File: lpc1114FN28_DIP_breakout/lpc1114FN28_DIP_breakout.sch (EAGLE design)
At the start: 17 parts, among them Q1 12MHz

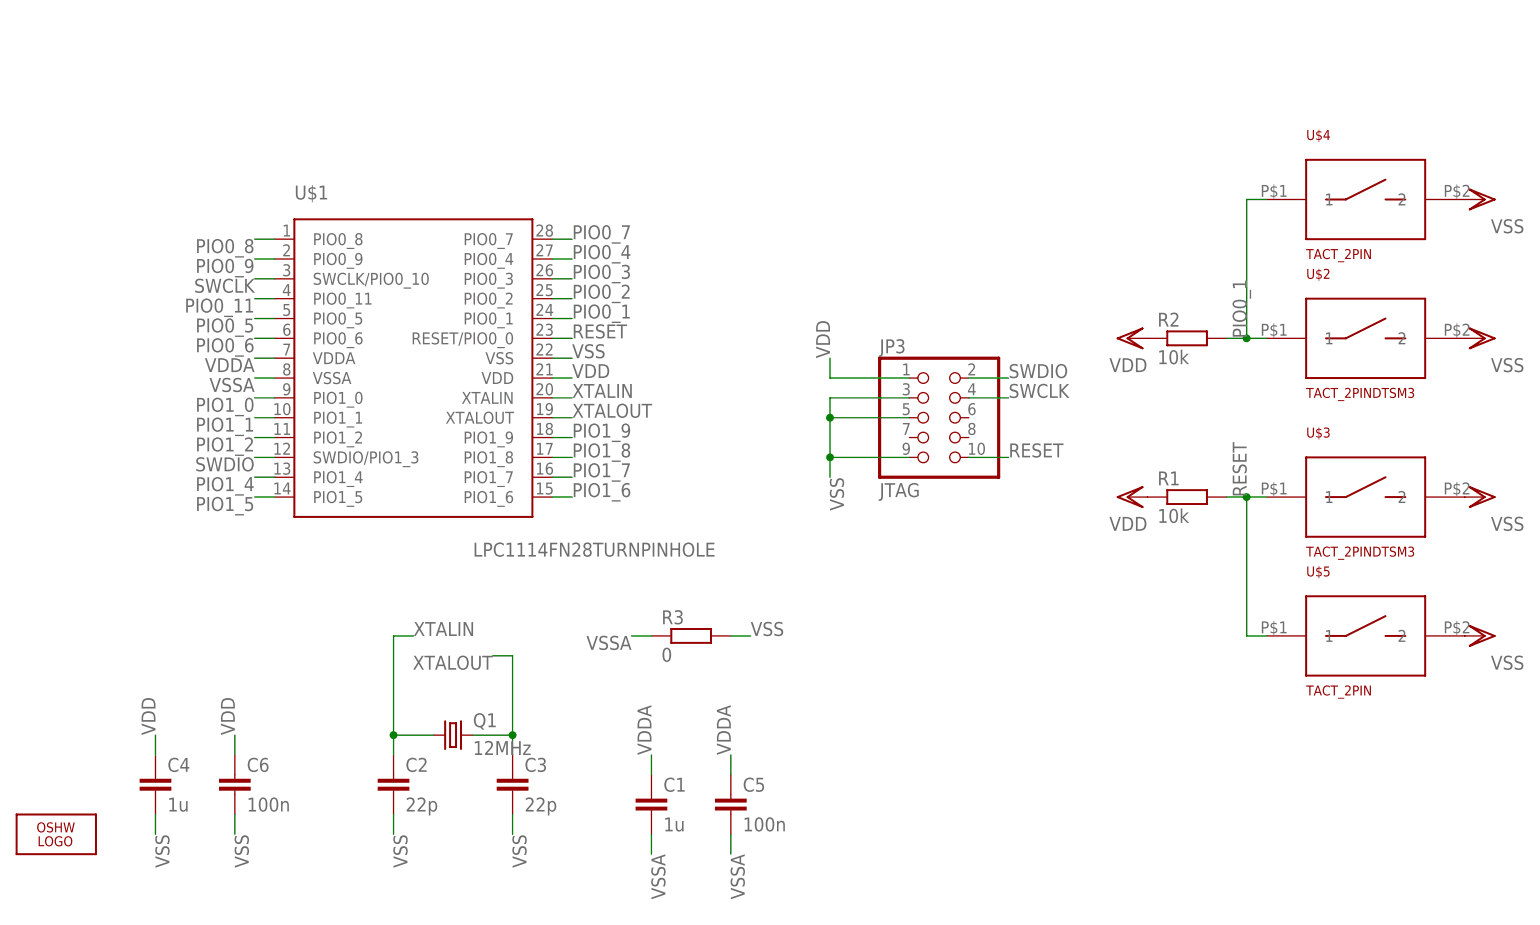
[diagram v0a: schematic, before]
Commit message: * more work on LPC1114FN28 PDIP breakout
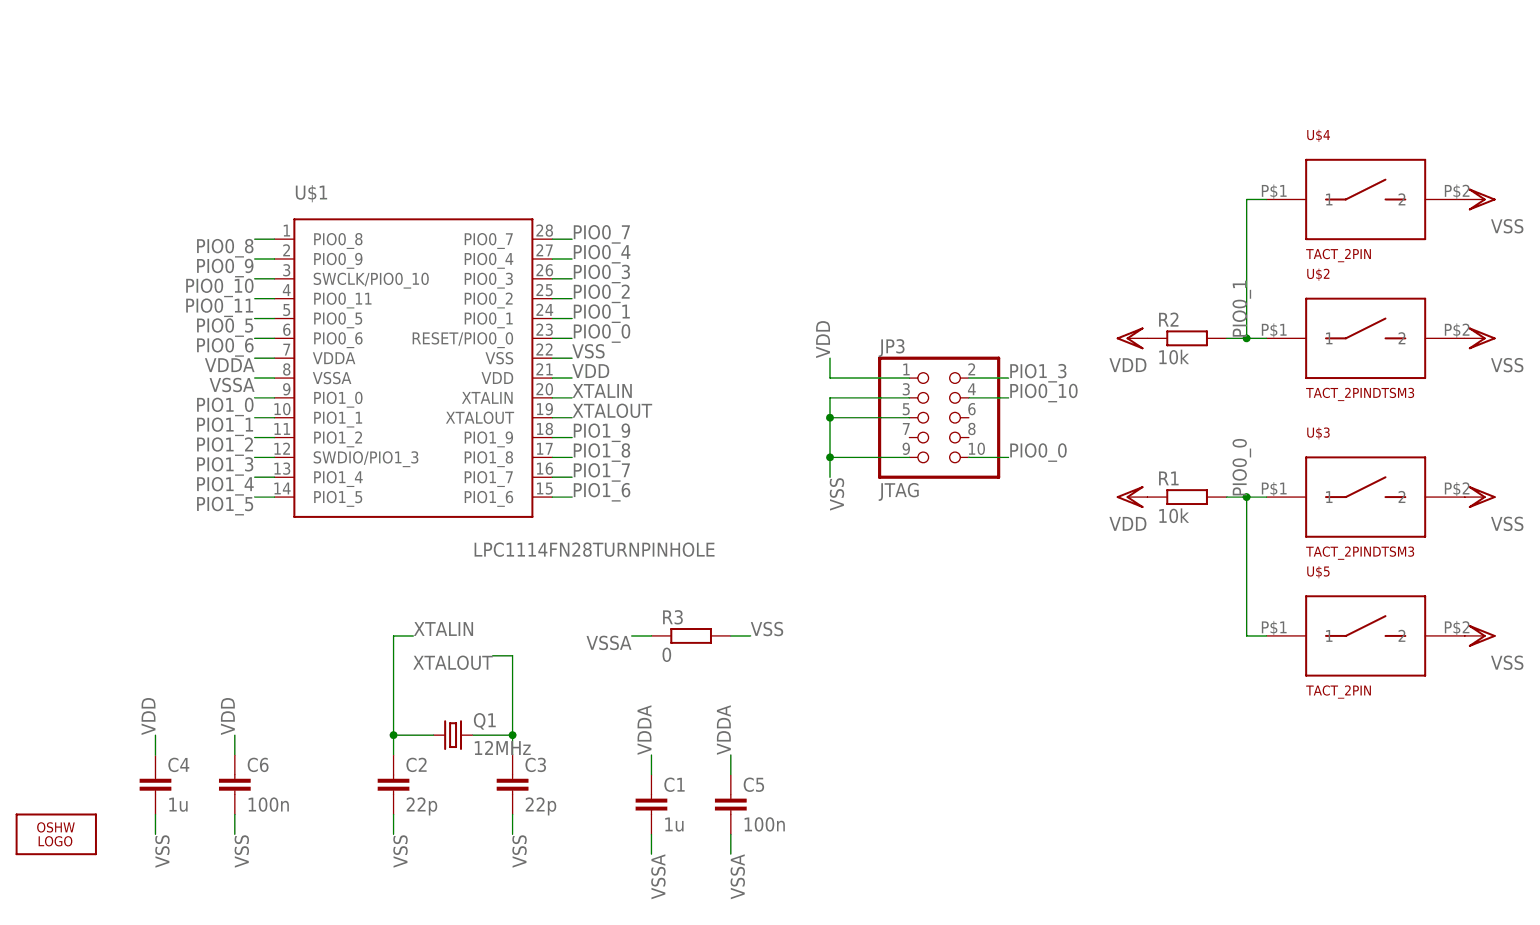
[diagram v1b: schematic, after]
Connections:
- net RESET renamed PIO0_0
- net SWCLK renamed PIO0_10
- net SWDIO renamed PIO1_3
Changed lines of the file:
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@@
-</segment>
-</net>
-<net name="SWCLK" class="0">
-<segment>
-<pinref part="U$1" gate="G$1" pin="SWCLK/PIO0_10"/>
-<wire x1="48.26" y1="81.28" x2="45.72" y2="81.28" width="0.1524" layer="91"/>
-<label x="45.72" y="81.28" size="1.778" layer="95" rot="R180"/>
-</segment>
-<segment>
-<pinref part="JP3" gate="A" pin="4"/>
-<wire x1="137.16" y1="66.04" x2="142.24" y2="66.04" width="0.1524" layer="91"/>
-<label x="142.24" y="66.04" size="1.778" layer="95"/>
 </segment>
 </net>
@@
 <wire x1="48.26" y1="60.96" x2="45.72" y2="60.96" width="0.1524" layer="91"/>
 <label x="45.72" y="60.96" size="1.778" layer="95" rot="R180"/>
-</segment>
-</net>
-<net name="SWDIO" class="0">
-<segment>
-<pinref part="U$1" gate="G$1" pin="SWDIO/PIO1_3"/>
-<wire x1="48.26" y1="58.42" x2="45.72" y2="58.42" width="0.1524" layer="91"/>
-<label x="45.72" y="58.42" size="1.778" layer="95" rot="R180"/>
-</segment>
-<segment>
-<pinref part="JP3" gate="A" pin="2"/>
-<wire x1="137.16" y1="68.58" x2="142.24" y2="68.58" width="0.1524" layer="91"/>
-<label x="142.24" y="68.58" size="1.778" layer="95"/>
 </segment>
 </net>
@@
 </segment>
 </net>
-<net name="RESET" class="0">
+<net name="PIO0_1" class="0">
+<segment>
+<pinref part="U$1" gate="G$1" pin="PIO0_1"/>
+<wire x1="83.82" y1="76.2" x2="86.36" y2="76.2" width="0.1524" layer="91"/>
+<label x="86.36" y="76.2" size="1.778" layer="95"/>
+</segment>
+<segment>
+<pinref part="R2" gate="G$1" pin="2"/>
+<wire x1="170.18" y1="73.66" x2="172.72" y2="73.66" width="0.1524" layer="91"/>
+<label x="172.72" y="73.66" size="1.778" layer="95" rot="R90"/>
+<pinref part="U$2" gate="G$1" pin="1"/>
+<pinref part="U$4" gate="G$1" pin="1"/>
+<wire x1="172.72" y1="73.66" x2="175.26" y2="73.66" width="0.1524" layer="91"/>
+<wire x1="175.26" y1="91.44" x2="172.72" y2="91.44" width="0.1524" layer="91"/>
+<wire x1="172.72" y1="91.44" x2="172.72" y2="73.66" width="0.1524" layer="91"/>
+<junction x="172.72" y="73.66"/>
+</segment>
+</net>
+<net name="PIO0_4" class="0">
+<segment>
+<pinref part="U$1" gate="G$1" pin="PIO0_4"/>
+<wire x1="83.82" y1="83.82" x2="86.36" y2="83.82" width="0.1524" layer="91"/>
+<label x="86.36" y="83.82" size="1.778" layer="95"/>
+</segment>
+</net>
+<net name="PIO0_7" class="0">
+<segment>
+<pinref part="U$1" gate="G$1" pin="PIO0_7"/>
+<wire x1="83.82" y1="86.36" x2="86.36" y2="86.36" width="0.1524" layer="91"/>
+<label x="86.36" y="86.36" size="1.778" layer="95"/>
+</segment>
+</net>
+<net name="PIO0_10" class="0">
+<segment>
+<pinref part="U$1" gate="G$1" pin="SWCLK/PIO0_10"/>
+<wire x1="48.26" y1="81.28" x2="45.72" y2="81.28" width="0.1524" layer="91"/>
+<label x="45.72" y="81.28" size="1.778" layer="95" rot="R180"/>
+</segment>
+<segment>
+<pinref part="JP3" gate="A" pin="4"/>
+<wire x1="137.16" y1="66.04" x2="142.24" y2="66.04" width="0.1524" layer="91"/>
+<label x="142.24" y="66.04" size="1.778" layer="95"/>
+</segment>
+</net>
+<net name="PIO1_3" class="0">
+<segment>
+<pinref part="U$1" gate="G$1" pin="SWDIO/PIO1_3"/>
+<wire x1="48.26" y1="58.42" x2="45.72" y2="58.42" width="0.1524" layer="91"/>
+<label x="45.72" y="58.42" size="1.778" layer="95" rot="R180"/>
+</segment>
+<segment>
+<pinref part="JP3" gate="A" pin="2"/>
+<wire x1="137.16" y1="68.58" x2="142.24" y2="68.58" width="0.1524" layer="91"/>
+<label x="142.24" y="68.58" size="1.778" layer="95"/>
+</segment>
+</net>
+<net name="PIO0_0" class="0">
 <segment>
 <pinref part="U$1" gate="G$1" pin="RESET/PIO0_0"/>
 <wire x1="83.82" y1="73.66" x2="86.36" y2="73.66" width="0.1524" layer="91"/>
 <label x="86.36" y="73.66" size="1.778" layer="95"/>
+</segment>
+<segment>
+<pinref part="JP3" gate="A" pin="10"/>
+<wire x1="137.16" y1="58.42" x2="142.24" y2="58.42" width="0.1524" layer="91"/>
+<label x="142.24" y="58.42" size="1.778" layer="95"/>
 </segment>
 <segment>
@@
 <junction x="172.72" y="53.34"/>
 </segment>
-<segment>
-<pinref part="JP3" gate="A" pin="10"/>
-<wire x1="137.16" y1="58.42" x2="142.24" y2="58.42" width="0.1524" layer="91"/>
-<label x="142.24" y="58.42" size="1.778" layer="95"/>
-</segment>
-</net>
-<net name="PIO0_1" class="0">
-<segment>
-<pinref part="U$1" gate="G$1" pin="PIO0_1"/>
-<wire x1="83.82" y1="76.2" x2="86.36" y2="76.2" width="0.1524" layer="91"/>
-<label x="86.36" y="76.2" size="1.778" layer="95"/>
-</segment>
-<segment>
-<pinref part="R2" gate="G$1" pin="2"/>
-<wire x1="170.18" y1="73.66" x2="172.72" y2="73.66" width="0.1524" layer="91"/>
-<label x="172.72" y="73.66" size="1.778" layer="95" rot="R90"/>
-<pinref part="U$2" gate="G$1" pin="1"/>
-<pinref part="U$4" gate="G$1" pin="1"/>
-<wire x1="172.72" y1="73.66" x2="175.26" y2="73.66" width="0.1524" layer="91"/>
-<wire x1="175.26" y1="91.44" x2="172.72" y2="91.44" width="0.1524" layer="91"/>
-<wire x1="172.72" y1="91.44" x2="172.72" y2="73.66" width="0.1524" layer="91"/>
-<junction x="172.72" y="73.66"/>
-</segment>
-</net>
-<net name="PIO0_4" class="0">
-<segment>
-<pinref part="U$1" gate="G$1" pin="PIO0_4"/>
-<wire x1="83.82" y1="83.82" x2="86.36" y2="83.82" width="0.1524" layer="91"/>
-<label x="86.36" y="83.82" size="1.778" layer="95"/>
-</segment>
-</net>
-<net name="PIO0_7" class="0">
-<segment>
-<pinref part="U$1" gate="G$1" pin="PIO0_7"/>
-<wire x1="83.82" y1="86.36" x2="86.36" y2="86.36" width="0.1524" layer="91"/>
-<label x="86.36" y="86.36" size="1.778" layer="95"/>
-</segment>
-</net>
+</net>

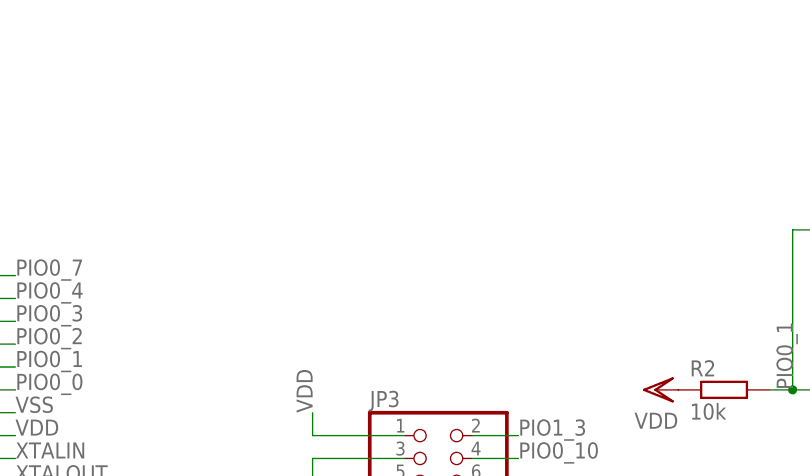
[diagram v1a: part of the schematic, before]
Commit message: * added final bits and smashed the components
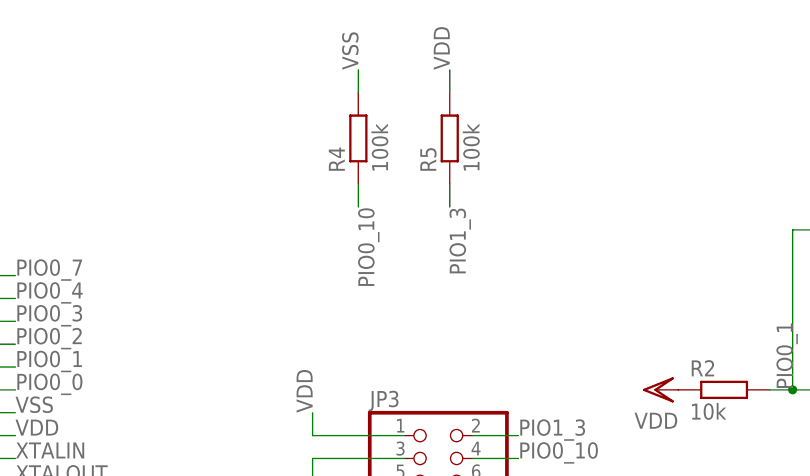
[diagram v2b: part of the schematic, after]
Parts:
- added R4, R5: 100k, bart_rcl:R-EU_R0603
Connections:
- net PIO0_10: now also R4.1
- net PIO1_3: now also R5.1
- net VDD: now also R5.2
- net VSS: now also R4.2
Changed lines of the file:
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@@
 <grid distance="0.1" unitdist="inch" unit="inch" style="lines" multiple="1" display="no" altdistance="0.01" altunitdist="inch" altunit="inch"/>
 <layers>
-<layer number="1" name="Top" color="4" fill="1" visible="yes" active="no"/>
-<layer number="16" name="Bottom" color="1" fill="1" visible="yes" active="no"/>
-<layer number="17" name="Pads" color="2" fill="1" visible="yes" active="no"/>
-<layer number="18" name="Vias" color="2" fill="1" visible="yes" active="no"/>
-<layer number="19" name="Unrouted" color="6" fill="1" visible="yes" active="no"/>
-<layer number="20" name="Dimension" color="15" fill="1" visible="yes" active="no"/>
-<layer number="21" name="tPlace" color="7" fill="1" visible="yes" active="no"/>
-<layer number="22" name="bPlace" color="7" fill="1" visible="yes" active="no"/>
-<layer number="23" name="tOrigins" color="15" fill="1" visible="yes" active="no"/>
-<layer number="24" name="bOrigins" color="15" fill="1" visible="yes" active="no"/>
-<layer number="25" name="tNames" color="7" fill="1" visible="yes" active="no"/>
-<layer number="26" name="bNames" color="7" fill="1" visible="yes" active="no"/>
-<layer number="27" name="tValues" color="7" fill="1" visible="yes" active="no"/>
-<layer number="28" name="bValues" color="7" fill="1" visible="yes" active="no"/>
+<layer number="1" name="Top" color="4" fill="1" visible="no" active="no"/>
+<layer number="16" name="Bottom" color="1" fill="1" visible="no" active="no"/>
+<layer number="17" name="Pads" color="2" fill="1" visible="no" active="no"/>
+<layer number="18" name="Vias" color="2" fill="1" visible="no" active="no"/>
+<layer number="19" name="Unrouted" color="6" fill="1" visible="no" active="no"/>
+<layer number="20" name="Dimension" color="15" fill="1" visible="no" active="no"/>
+<layer number="21" name="tPlace" color="7" fill="1" visible="no" active="no"/>
+<layer number="22" name="bPlace" color="7" fill="1" visible="no" active="no"/>
+<layer number="23" name="tOrigins" color="15" fill="1" visible="no" active="no"/>
+<layer number="24" name="bOrigins" color="15" fill="1" visible="no" active="no"/>
+<layer number="25" name="tNames" color="7" fill="1" visible="no" active="no"/>
+<layer number="26" name="bNames" color="7" fill="1" visible="no" active="no"/>
+<layer number="27" name="tValues" color="7" fill="1" visible="no" active="no"/>
+<layer number="28" name="bValues" color="7" fill="1" visible="no" active="no"/>
 <layer number="29" name="tStop" color="7" fill="3" visible="no" active="no"/>
 <layer number="30" name="bStop" color="7" fill="6" visible="no" active="no"/>
@@
 <layer number="35" name="tGlue" color="7" fill="4" visible="no" active="no"/>
 <layer number="36" name="bGlue" color="7" fill="5" visible="no" active="no"/>
-<layer number="37" name="tTest" color="7" fill="1" visible="yes" active="no"/>
-<layer number="38" name="bTest" color="7" fill="1" visible="yes" active="no"/>
+<layer number="37" name="tTest" color="7" fill="1" visible="no" active="no"/>
+<layer number="38" name="bTest" color="7" fill="1" visible="no" active="no"/>
 <layer number="39" name="tKeepout" color="4" fill="11" visible="no" active="no"/>
 <layer number="40" name="bKeepout" color="1" fill="11" visible="no" active="no"/>
@@
 <layer number="44" name="Drills" color="7" fill="1" visible="no" active="no"/>
 <layer number="45" name="Holes" color="7" fill="1" visible="no" active="no"/>
-<layer number="46" name="Milling" color="3" fill="1" visible="yes" active="no"/>
-<layer number="47" name="Measures" color="7" fill="1" visible="yes" active="no"/>
-<layer number="48" name="Document" color="7" fill="1" visible="yes" active="no"/>
-<layer number="49" name="Reference" color="7" fill="1" visible="yes" active="no"/>
-<layer number="50" name="dxf" color="7" fill="1" visible="yes" active="no"/>
-<layer number="51" name="tDocu" color="7" fill="1" visible="yes" active="no"/>
-<layer number="52" name="bDocu" color="7" fill="1" visible="yes" active="no"/>
-<layer number="53" name="tGND_GNDA" color="7" fill="9" visible="yes" active="no"/>
-<layer number="54" name="bGND_GNDA" color="1" fill="9" visible="yes" active="no"/>
-<layer number="56" name="wert" color="7" fill="1" visible="yes" active="no"/>
+<layer number="46" name="Milling" color="3" fill="1" visible="no" active="no"/>
+<layer number="47" name="Measures" color="7" fill="1" visible="no" active="no"/>
+<layer number="48" name="Document" color="7" fill="1" visible="no" active="no"/>
+<layer number="49" name="Reference" color="7" fill="1" visible="no" active="no"/>
+<layer number="50" name="dxf" color="7" fill="1" visible="no" active="no"/>
+<layer number="51" name="tDocu" color="7" fill="1" visible="no" active="no"/>
+<layer number="52" name="bDocu" color="7" fill="1" visible="no" active="no"/>
+<layer number="53" name="tGND_GNDA" color="7" fill="9" visible="no" active="no"/>
+<layer number="54" name="bGND_GNDA" color="1" fill="9" visible="no" active="no"/>
+<layer number="56" name="wert" color="7" fill="1" visible="no" active="no"/>
 <layer number="90" name="Modules" color="5" fill="1" visible="yes" active="yes"/>
 <layer number="91" name="Nets" color="2" fill="1" visible="yes" active="yes"/>
@@
 <part name="C5" library="SquantorRCL" deviceset="C-EU" device="C0603K" value="100n"/>
 <part name="R3" library="SquantorRCL" deviceset="R-EU_" device="R0603" value="0"/>
+<part name="R4" library="bart_rcl" deviceset="R-EU_" device="R0603" value="100k"/>
+<part name="R5" library="bart_rcl" deviceset="R-EU_" device="R0603" value="100k"/>
 </parts>
 <sheets>
@@
 <instance part="C5" gate="G$1" x="106.68" y="15.24"/>
 <instance part="R3" gate="G$1" x="101.6" y="35.56"/>
+<instance part="R4" gate="G$1" x="124.46" y="101.6" rot="R90"/>
+<instance part="R5" gate="G$1" x="134.62" y="101.6" rot="R90"/>
 </instances>
 <busses>
@@
 <label x="119.38" y="55.88" size="1.778" layer="95" rot="R270"/>
 </segment>
+<segment>
+<pinref part="R4" gate="G$1" pin="2"/>
+<wire x1="124.46" y1="106.68" x2="124.46" y2="109.22" width="0.1524" layer="91"/>
+<label x="124.46" y="109.22" size="1.778" layer="95" rot="R90"/>
+</segment>
 </net>
 <net name="VDD" class="0">
@@
 <wire x1="119.38" y1="68.58" x2="119.38" y2="71.12" width="0.1524" layer="91"/>
 <label x="119.38" y="71.12" size="1.778" layer="95" rot="R90"/>
+</segment>
+<segment>
+<pinref part="R5" gate="G$1" pin="2"/>
+<wire x1="134.62" y1="106.68" x2="134.62" y2="109.22" width="0.1524" layer="91"/>
+<label x="134.62" y="109.22" size="1.778" layer="95" rot="R90"/>
 </segment>
 </net>
@@
 <label x="142.24" y="66.04" size="1.778" layer="95"/>
 </segment>
+<segment>
+<pinref part="R4" gate="G$1" pin="1"/>
+<wire x1="124.46" y1="96.52" x2="124.46" y2="93.98" width="0.1524" layer="91"/>
+<label x="124.46" y="93.98" size="1.778" layer="95" rot="R270"/>
+</segment>
 </net>
 <net name="PIO1_3" class="0">
@@
 <label x="142.24" y="68.58" size="1.778" layer="95"/>
 </segment>
-</net>
+<segment>
+<pinref part="R5" gate="G$1" pin="1"/>
+<wire x1="134.62" y1="96.52" x2="134.62" y2="93.98" width="0.1524" layer="91"/>
+<label x="134.62" y="93.98" size="1.778" layer="95" rot="R270"/>
+</segment>
+</net>
